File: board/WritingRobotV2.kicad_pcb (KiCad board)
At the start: 2 copper layers, 61.5 x 55 mm, 7 parts, among them J1 Conn_01x02_Socket, J2 Conn_01x04_Pin, J3 Conn_01x04_Pin, J4 Conn_01x06_Socket

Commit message: Board updated
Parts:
- added C1: C_Polarized, Capacitor_THT:CP_Radial_D5.0mm_P2.50mm, F.Cu at (121.5, 45.5)
- added C2: C, Capacitor_THT:C_Rect_L4.0mm_W2.5mm_P2.50mm, F.Cu at (127.0, 53.2)
- added H1: MountingHole, MountingHole:MountingHole_4.3mm_M4, F.Cu at (79.2, 93.5)
- added H3: MountingHole, MountingHole:MountingHole_4.3mm_M4, F.Cu at (77.7, 44.7)
- added H4: MountingHole, MountingHole:MountingHole_4.3mm_M4, F.Cu at (131.6, 65.0)
- added R1: R, Resistor_THT:R_Axial_DIN0411_L9.9mm_D3.6mm_P7.62mm_Vertical, F.Cu at (126.5, 49.0)
- moved J1 23.8 mm to (134.0, 56.5), turned to 180 degrees
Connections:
- net Net-(A1-D10) renamed CS
- net Net-(A1-D3) renamed DIR_M2
- net Net-(A1-D4) renamed STEP_M2
- net Net-(A1-D5) renamed DIR_M1
- net Net-(A1-D6) renamed STEP_M1
- net Net-(A1-MISO) renamed MISO
- net Net-(A1-MOSI) renamed MOSI
- net Net-(A1-SCK) renamed SCK
- A2 pad 10: unconnected-(A2-MS1-Pad10) -> +5V
- A2 pad 11: unconnected-(A2-MS2-Pad11) -> +5V
- A2 pad 12: unconnected-(A2-MS3-Pad12) -> +5V
- A2 pad 13: unconnected-(A2-~{RESET}-Pad13) -> Net-(A2-~{RESET})
- A2 pad 14: unconnected-(A2-~{SLEEP}-Pad14) -> Net-(A2-~{RESET})
- A3 pad 10: unconnected-(A3-MS1-Pad10) -> +5V
- A3 pad 11: unconnected-(A3-MS2-Pad11) -> +5V
- A3 pad 12: unconnected-(A3-MS3-Pad12) -> +5V
- A3 pad 13: unconnected-(A3-~{RESET}-Pad13) -> Net-(A3-~{RESET})
- A3 pad 14: unconnected-(A3-~{SLEEP}-Pad14) -> Net-(A3-~{RESET})
- J1 pad 2: +12V -> Net-(J1-Pin_2)
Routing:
- net +5V: track 124.6 -> 161.0 mm
- net GND: track 139.8 -> 174.1 mm
- net Net-(J1-Pin_2): track 0.00 -> 5.05 mm
- net +12V: track 102.7 -> 107.2 mm
- net Net-(A2-~{RESET}): track 0.00 -> 2.54 mm
- net Net-(A3-~{RESET}): track 0.00 -> 2.54 mm
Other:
- board text added: "+"
- board text added: "-"
- board text added: "A4988"
- board text added: "Arduino nano"
- board text added: "CLK MOSI MISO CS GND VCC"
- board text added: "Motor 1"
- board text added: "Motor 2"

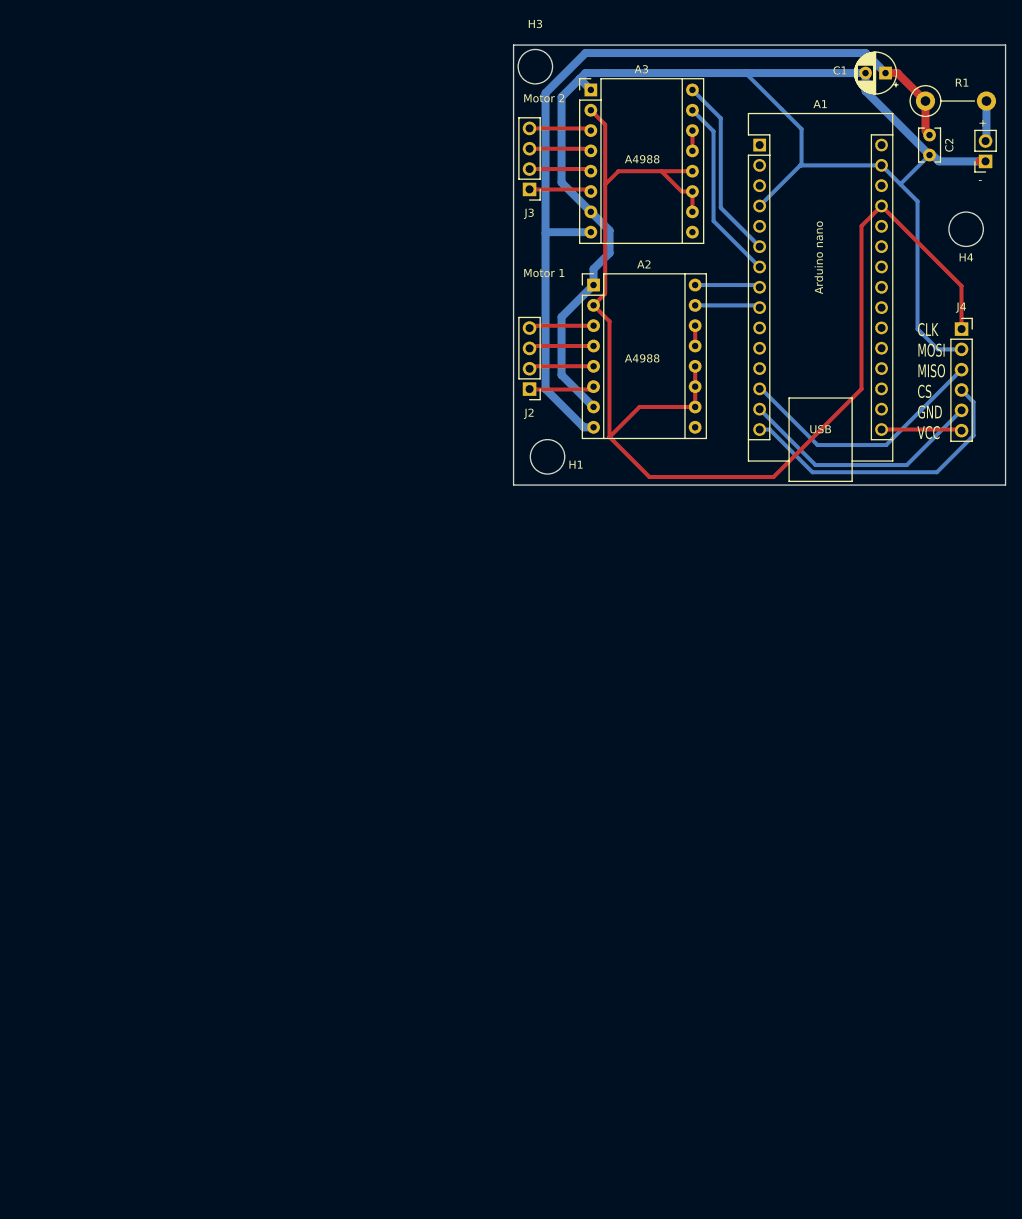
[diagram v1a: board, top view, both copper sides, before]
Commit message: Board to stm32
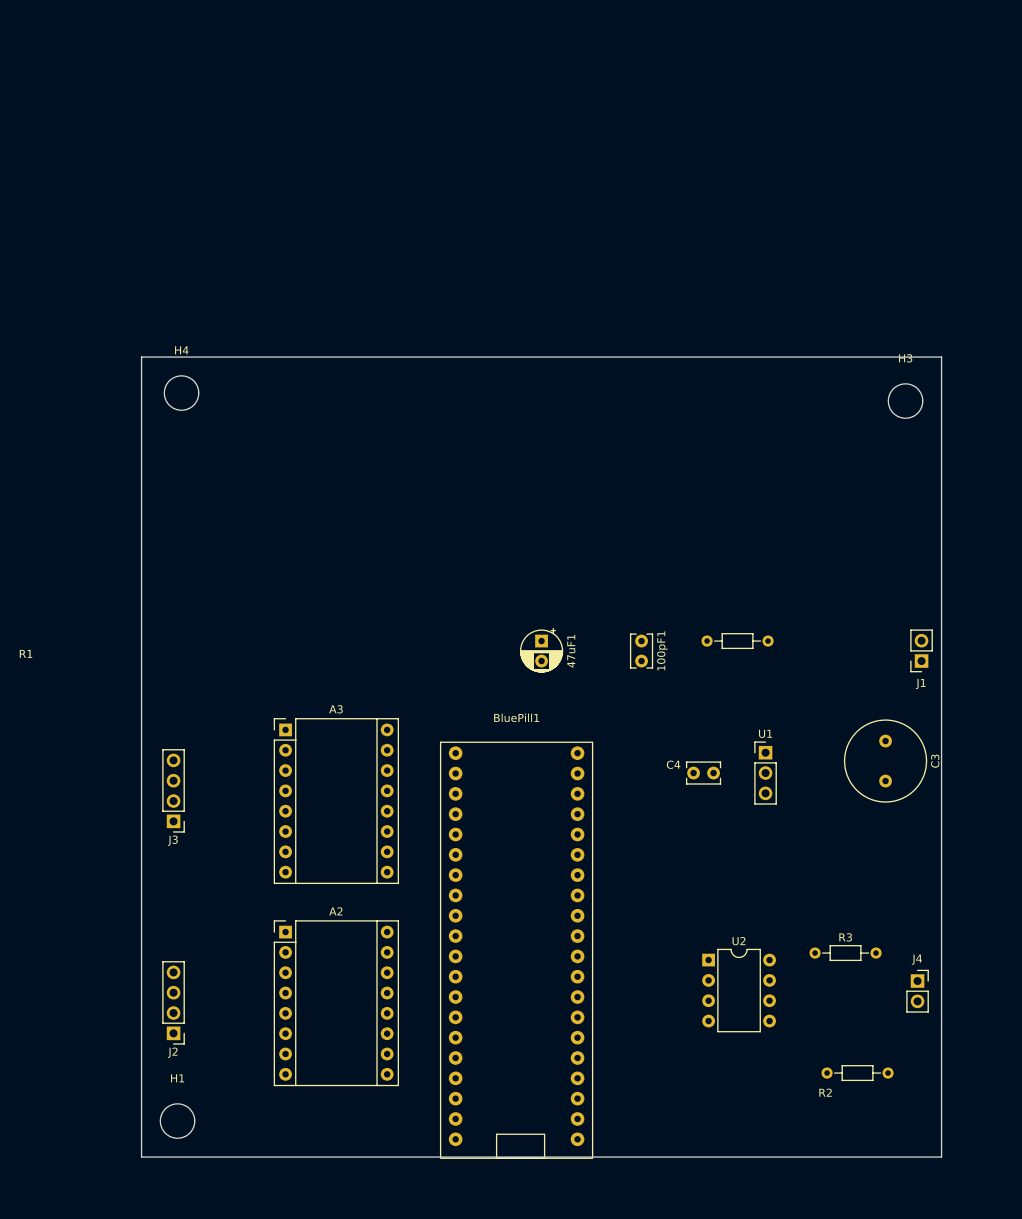
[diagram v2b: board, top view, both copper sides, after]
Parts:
- removed A1: Arduino_Nano_Every, Module:Arduino_Nano
- removed C1: C_Polarized, Capacitor_THT:CP_Radial_D5.0mm_P2.50mm
- removed C2: C, Capacitor_THT:C_Rect_L4.0mm_W2.5mm_P2.50mm
- added 100pF1: C, Capacitor_THT:C_Rect_L4.0mm_W2.5mm_P2.50mm, F.Cu at (91.0, 116.5)
- added 47uF1: C_Polarized, Capacitor_THT:CP_Radial_D5.0mm_P2.50mm, F.Cu at (78.5, 116.5)
- added BluePill1: ~, STM32_Bluepill:BluePill, F.Cu at (75.4, 154.7)
- added C3: 0.22uF, Capacitor_THT:C_Radial_D10.0mm_H16.0mm_P5.00mm, F.Cu at (121.5, 129.0)
- added C4: 0.1uF, Capacitor_THT:C_Rect_L4.0mm_W2.5mm_P2.50mm, F.Cu at (97.5, 133.0)
- added R2: 60, Resistor_THT:R_Axial_DIN0204_L3.6mm_D1.6mm_P7.62mm_Horizontal, F.Cu at (114.2, 170.5)
- added R3: 60, Resistor_THT:R_Axial_DIN0204_L3.6mm_D1.6mm_P7.62mm_Horizontal, F.Cu at (112.7, 155.5)
- added U1: L7805, Connector_PinHeader_2.54mm:PinHeader_1x03_P2.54mm_Vertical, F.Cu at (106.5, 130.5)
- added U2: MCP2551-I-P, Package_DIP:DIP-8_W7.62mm, F.Cu at (99.4, 156.4)
- J1: value Conn_01x02_Socket -> POWER-INPUT
- J2: value Conn_01x04_Pin -> MOTOR-1-OUTPUT
- J3: value Conn_01x04_Pin -> MOTOR-2-OUTPUT
- J4: value Conn_01x06_Socket -> CAN-INPUT; footprint Connector_PinSocket_2.54mm:PinSocket_1x06_P2.54mm_Vertical -> Connector_PinSocket_2.54mm:PinSocket_1x02_P2.54mm_Vertical
- R1: footprint Resistor_THT:R_Axial_DIN0411_L9.9mm_D3.6mm_P7.62mm_Vertical -> Resistor_THT:R_Axial_DIN0204_L3.6mm_D1.6mm_P7.62mm_Horizontal
- moved H4 100.2 mm to (33.5, 85.5)
- moved H1 95.0 mm to (33.0, 176.5)
- moved J2 92.0 mm to (32.5, 165.5)
- moved J3 90.7 mm to (32.5, 139.0)
- moved A2 89.6 mm to (46.5, 152.9)
- moved A3 88.6 mm to (46.5, 127.6)
- moved J4 81.7 mm to (125.5, 159.0)
- moved R1 72.8 mm to (99.2, 116.5)
- moved J1 63.0 mm to (126.0, 119.0)
- moved H3 62.4 mm to (124.0, 86.5)
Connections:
- J4 pad 1: +5V -> Net-(J4-Pin_1)
- J4 pad 2: GND -> Net-(J4-Pin_2)
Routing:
- net GND: track 174.1 -> 0.00 mm
- net +5V: track 161.0 -> 0.00 mm
- net +12V: track 107.2 -> 0.00 mm
- net MISO: track 37.2 -> 0.00 mm
- net CS: track 32.0 -> 0.00 mm
- net MOSI: track 31.2 -> 0.00 mm
- net STEP_M2: track 23.1 -> 0.00 mm
- net DIR_M2: track 23.1 -> 0.00 mm
- net SCK: track 10.1 -> 0.00 mm
- net DIR_M1: track 8.18 -> 0.00 mm
- net STEP_M1: track 8.18 -> 0.00 mm
- net Net-(A2-2B): track 8.16 -> 0.00 mm
- net Net-(A2-2A): track 8.12 -> 0.00 mm
- net Net-(A2-1B): track 8.12 -> 0.00 mm
- net Net-(A2-1A): track 8.12 -> 0.00 mm
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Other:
- board size 61.5 x 55 mm -> 100 x 100 mm
- board text removed: "+"
- board text removed: "-"
- board text removed: "A4988"
- board text removed: "Arduino nano"
- board text removed: "CLK MOSI MISO CS GND VCC"
- board text removed: "Motor 1"
- board text removed: "Motor 2"

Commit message: Board updated to STM32
Other files in rework
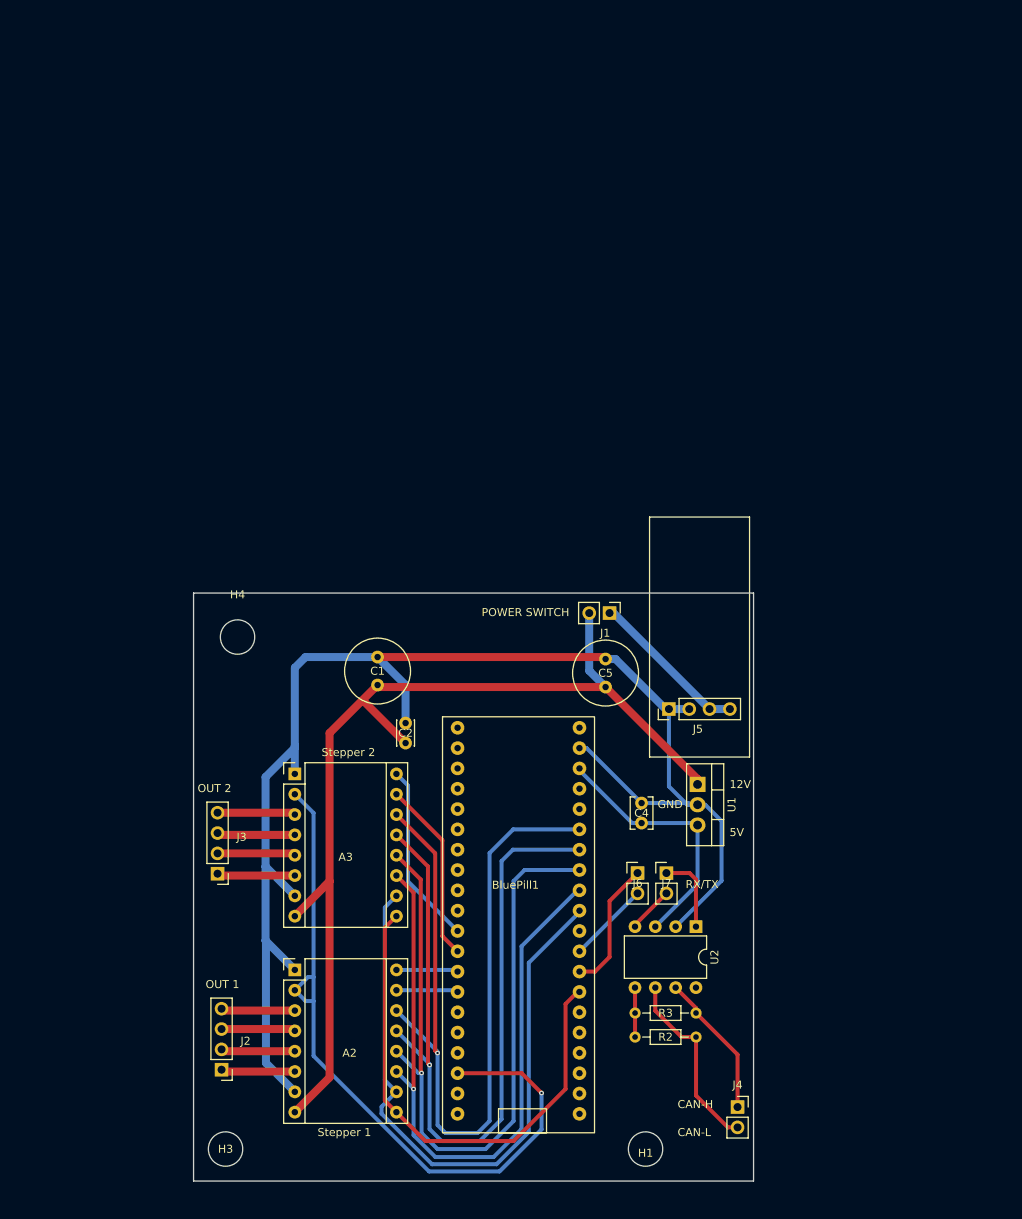
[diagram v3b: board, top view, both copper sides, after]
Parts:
- removed C3: 0.22uF, Capacitor_THT:C_Radial_D10.0mm_H16.0mm_P5.00mm
- removed R1: R, Resistor_THT:R_Axial_DIN0204_L3.6mm_D1.6mm_P7.62mm_Horizontal
- added C5: 47 uF, Capacitor_THT:C_Radial_D8.0mm_H11.5mm_P3.50mm, F.Cu at (86.5, 122.2)
- added J5: POWER_INPUT, Connector_PinHeader_2.54mm:PinHeader_1x04_P2.54mm_Vertical, F.Cu at (94.4, 125.0)
- added J6: Conn_01x02_Pin, Connector_PinHeader_2.54mm:PinHeader_1x02_P2.54mm_Vertical, F.Cu at (90.5, 145.5)
- added J7: Conn_01x02_Pin, Connector_PinHeader_2.54mm:PinHeader_1x02_P2.54mm_Vertical, F.Cu at (94.1, 145.5)
- C1: renamed from 47uF1; value C_Polarized -> 47 uF; footprint Capacitor_THT:CP_Radial_D5.0mm_P2.50mm -> Capacitor_THT:C_Radial_D8.0mm_H11.5mm_P3.50mm
- C2: renamed from 100pF1; value C -> 100 nF; footprint Capacitor_THT:C_Rect_L4.0mm_W2.5mm_P2.50mm -> Capacitor_THT:C_Disc_D3.0mm_W2.0mm_P2.50mm
- C4: footprint Capacitor_THT:C_Rect_L4.0mm_W2.5mm_P2.50mm -> Capacitor_THT:C_Disc_D3.8mm_W2.6mm_P2.50mm
- J1: value POWER-INPUT -> PowerSwitch; footprint Connector_PinSocket_2.54mm:PinSocket_1x02_P2.54mm_Vertical -> Connector_PinHeader_2.54mm:PinHeader_1x02_P2.54mm_Vertical
- U1: footprint Connector_PinHeader_2.54mm:PinHeader_1x03_P2.54mm_Vertical -> Package_TO_SOT_THT:TO-220-3_Vertical
- moved H3 126.4 mm to (39.0, 180.0)
- moved H1 58.6 mm to (91.5, 180.0)
- moved J1 39.5 mm to (87.0, 113.0), turned to -90 degrees
- moved C2 32.1 mm to (61.5, 129.2), turned to 90 degrees
- moved H4 31.3 mm to (40.5, 116.0)
- moved J4 27.5 mm to (103.0, 174.8)
- moved R2 24.4 mm to (90.2, 166.0)
- moved R3 23.7 mm to (90.2, 163.0)
- moved C1 21.2 mm to (58.0, 122.0), turned to 90 degrees
- moved U1 9.38 mm to (98.0, 134.4), turned to -90 degrees
- moved C4 9.02 mm to (91.0, 139.2), turned to 90 degrees
- moved J3 8.55 mm to (38.0, 145.6)
- moved J2 7.52 mm to (38.5, 170.1)
- moved A3 5.62 mm to (47.7, 133.1)
- moved A2 4.87 mm to (47.7, 157.6)
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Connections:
- A2 pad 10: +5V -> MS3
- A2 pad 11: +5V -> MS2
- A2 pad 12: +5V -> MS1
- A2 pad 13: Net-(A2-~{RESET}) -> RESET_STEPPERS
- A2 pad 14: Net-(A2-~{RESET}) -> SLEEP_STEPPERS
- A2 pad 2: +5V -> 3.3V
- A2 pad 9: unconnected-(A2-~{ENABLE}-Pad9) -> Enable Steppers
- A3 pad 10: +5V -> MS3
- A3 pad 11: +5V -> MS2
- A3 pad 12: +5V -> MS1
- A3 pad 13: Net-(A3-~{RESET}) -> RESET_STEPPERS
- A3 pad 14: Net-(A3-~{RESET}) -> SLEEP_STEPPERS
- A3 pad 2: +5V -> 3.3V
- A3 pad 9: unconnected-(A3-~{ENABLE}-Pad9) -> Enable Steppers
- BluePill1 pad 18: unconnected-(BluePill1-3.3V-Pad18) -> 3.3V
- BluePill1 pad 26: unconnected-(BluePill1-B7-Pad26) -> SLEEP_STEPPERS
- BluePill1 pad 27: unconnected-(BluePill1-B6-Pad27) -> RESET_STEPPERS
- BluePill1 pad 28: unconnected-(BluePill1-B5-Pad28) -> MS1
- BluePill1 pad 29: unconnected-(BluePill1-B4-Pad29) -> MS2
- BluePill1 pad 30: unconnected-(BluePill1-B3-Pad30) -> MS3
- BluePill1 pad 32: TD -> TX
- BluePill1 pad 33: RD -> RX
- BluePill1 pad 34: unconnected-(BluePill1-A10-Pad34) -> Enable Steppers
- J1 pad 1: GND -> Net-(J1-Pin_1)
- J1 pad 2: Net-(J1-Pin_2) -> +12V
- U2 pad 1: TD -> Net-(J7-Pin_1)
- U2 pad 4: RD -> Net-(J7-Pin_2)
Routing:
- net GND: track 0.00 -> 183.8 mm
- net +12V: track 0.00 -> 127.8 mm
- net SLEEP_STEPPERS: track 0.00 -> 101.6 mm, vias 0 -> 1
- net RESET_STEPPERS: track 0.00 -> 97.6 mm, vias 0 -> 1
- net MS1: track 0.00 -> 92.7 mm, vias 0 -> 1
- net 3.3V: track 0.00 -> 92.3 mm, vias 0 -> 1
- net MS2: track 0.00 -> 85.2 mm, vias 0 -> 1
- net MS3: track 0.00 -> 82.1 mm
- net Enable Steppers: track 0.00 -> 63.8 mm
- net +5V: track 0.00 -> 32.8 mm
- net Net-(J4-Pin_2): track 0.00 -> 23.5 mm
- net STEP_M2: track 0.00 -> 22.8 mm
- net DIR_M2: track 0.00 -> 22.8 mm
- net Net-(J1-Pin_1): track 0.00 -> 20.0 mm
- net Net-(J4-Pin_1): track 0.00 -> 18.1 mm
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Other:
- board size 100 x 100 mm -> 70 x 73.5 mm
- board text added: "12V"
- board text added: "5V"
- board text added: "CAN-H"
- board text added: "CAN-L"
- board text added: "GND"
- board text added: "OUT 1"
- board text added: "OUT 2"
- board text added: "POWER SWITCH"
- board text added: "RX/TX"
- board text added: "Stepper 1"
- board text added: "Stepper 2"

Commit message: This was send to manufactory
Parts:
- added G***: LOGO, Logo:pikachu_small_3, B.Cu at (71.0, 143.0)
- added J10: DEBUG_5V, Connector_PinHeader_2.54mm:PinHeader_1x01_P2.54mm_Vertical, F.Cu at (103.0, 149.5)
- added J8: DEBUG_GND, Connector_PinHeader_2.54mm:PinHeader_1x01_P2.54mm_Vertical, F.Cu at (63.5, 113.0)
- added J9: DEBUG_12V, Connector_PinHeader_2.54mm:PinHeader_1x01_P2.54mm_Vertical, F.Cu at (51.0, 113.5)
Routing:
- net +5V: track 32.8 -> 44.9 mm
- net +12V: track 127.8 -> 139.2 mm
- net GND: track 183.8 -> 188.6 mm
- net Net-(J1-Pin_1): track 20.0 -> 20.7 mm
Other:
- board size 70 x 73.5 mm -> 70 x 75 mm
- board text added: "DBG 12V"
- board text added: "DBG GND"
- board text added: "DBG V5"
- board text added: "WTF it's alive?"
